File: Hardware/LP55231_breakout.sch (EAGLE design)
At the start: 13 parts

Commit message: PCB Work in progress.
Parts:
- removed LED3: LED-TRICOLOR-NO-COMPLCC-6-SMD, SparkFun-LED:LED-TRICOLOR-NO-COMPLCC-6-SMD
- added FD1, FD2: FIDUCIALUFIDUCIAL, SparkFun-Aesthetics:FIDUCIALUFIDUCIAL
- added J1, J2, J3: (no value), SparkFun-Connectors:M04NO_SILK_ALL_ROUND
- added J4: (no value), SparkFun-Connectors:M09NO_SILK
- added JP3: I2C-PULLUPS, SparkFun-Passives:JUMPER-PAD-3-NC_BY_PASTE
- added LED4: LED-TRICOLOR-5050NO_IC, SparkFun-LED:LED-TRICOLOR-5050NO_IC
- added R1, R2: 4.7K, SparkFun-Resistors:4.7KOHM-1/10W-1%(0603)
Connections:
- net N$16 renamed ADDR1
- net N$17 renamed ADDR0
- removed net N$1: LED3.RED, U$1.R3/D9
- removed net N$10: C1.1, U$1.VOUT
- removed net N$2: LED3.GRN, U$1.G3/D5
- removed net N$3: LED3.BLU, U$1.B3/D6
- removed net N$4: LED2.BLU, U$1.B2/D4
- removed net N$5: LED2.RED, U$1.R2/D8
- removed net N$6: LED2.GRN, U$1.G2/D3
- removed net N$7: LED1.RED, U$1.R1/D7
- removed net N$8: LED1.GRN, U$1.G1/D1
- removed net N$9: LED1.BLU, U$1.B1/D2
- new net B1: J1.4, LED1.BLU, U$1.B1/D2
- new net B2: J2.4, LED2.BLU, U$1.B2/D4
- new net B3: J3.4, LED4.BLU-A, U$1.B3/D6
- new net G1: J1.3, LED1.GRN, U$1.G1/D1
- new net G2: J2.3, LED2.GRN, U$1.G2/D3
- new net G3: J3.3, LED4.GRN-A, U$1.G3/D5
- new net N$15: U$1.INT
- new net N$18: U$1.TRIG
- new net N$19: U$1.EN
- new net N$20: U$1.CLK
- new net N$21: JP3.1, R2.2
- new net N$22: JP3.3, R1.2
- new net R1: J1.1, LED1.RED, U$1.R1/D7
- new net R2: J2.1, LED2.RED, U$1.R2/D8
- new net R3: J3.1, LED4.RED-A, U$1.R3/D9
- new net SCL: J4.4, R1.1, U$1.SCL
- new net SDA: J4.3, R2.1, U$1.SDA
- new net VOUT: C1.1, J4.9, U$1.VOUT
- net GND: now also J1.2, J2.2, J3.2, J4.1, LED4.BLU-C, LED4.GRN-C, LED4.RED-C; no longer LED3.BC, LED3.GC, LED3.RC
- net VCC: now also J4.2, JP3.2
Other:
- note added: "Disconnect JP3 to defeat onboard I2C pullup resistors"
- note added: "J1, J2, J3 are header pads for PTH RGB LEDs, such as COM-09264 or COM-00105"
- note added: "JP1, JP2 configure I2C Addresses: A1, A0 = address (hex) 0,0 - 0x32 0,1 - 0x33 1,0 - 0x34 1,1 - 0x35"
- note removed: "I2C Addresses: A1, A0: address (hex) 0,0 - 0x32 0,1 - 0x33 1,0 - 0x34 1,1 - 0x35"
- moved on the sheet: LED1, LED2

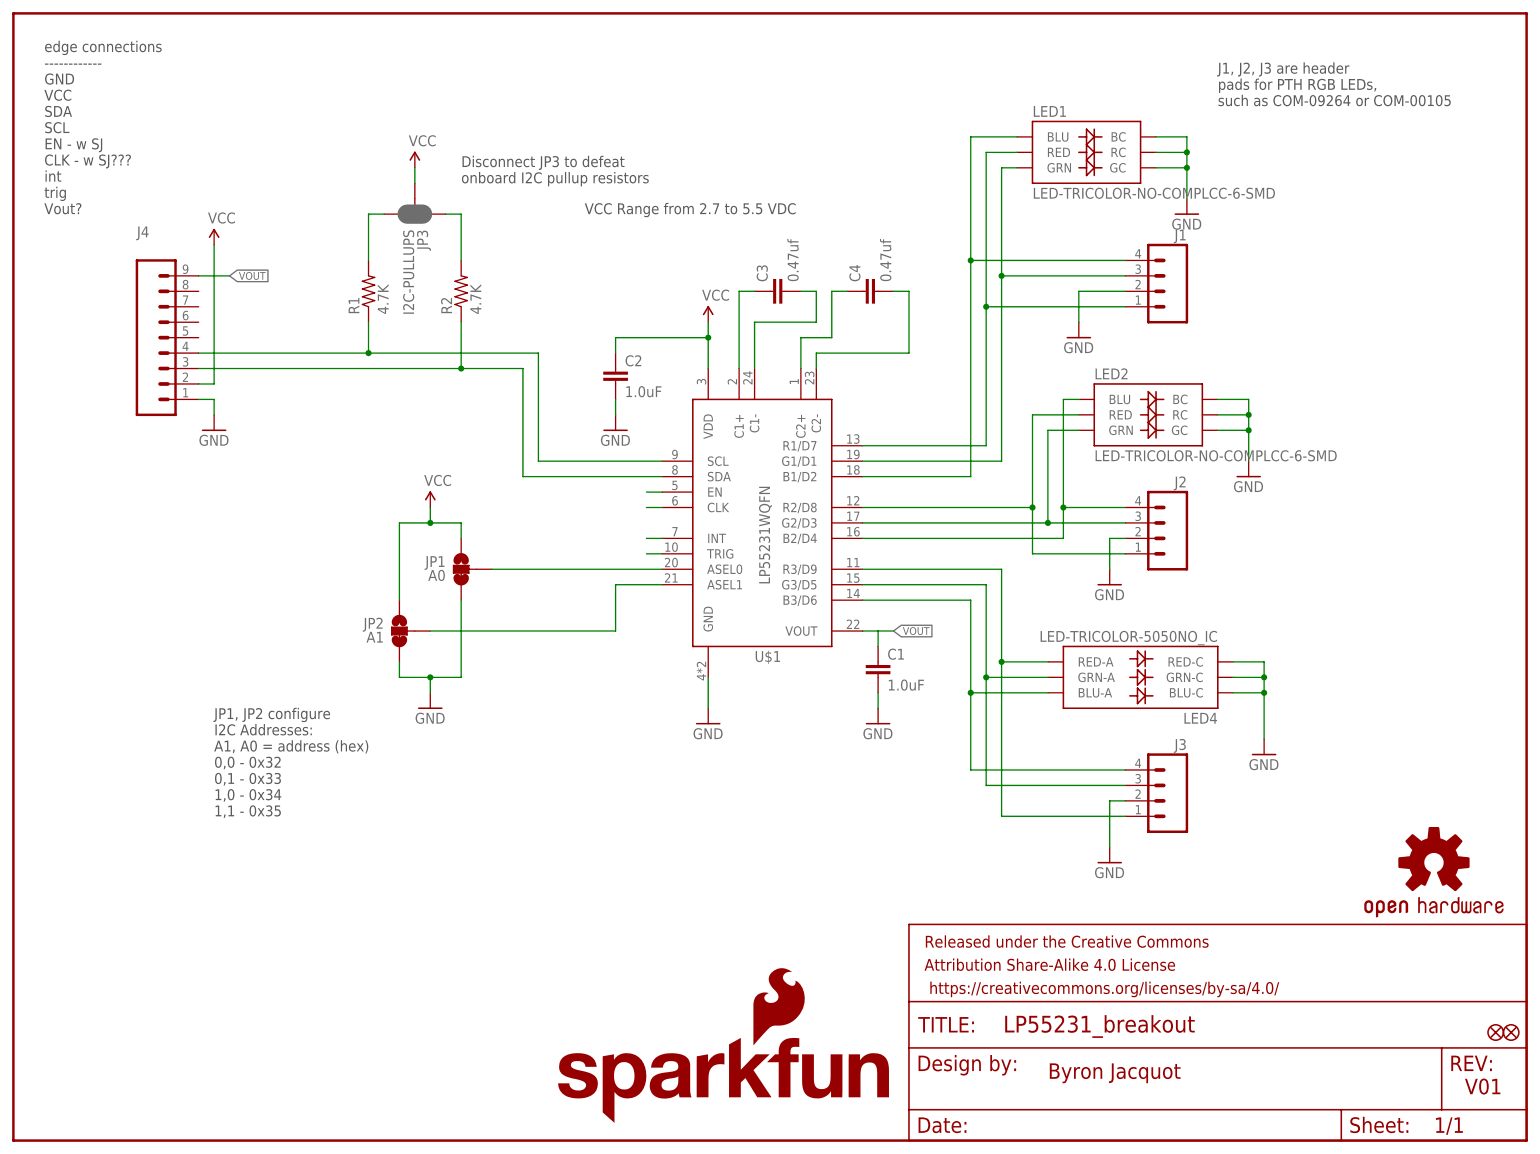
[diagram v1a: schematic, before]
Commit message: Incremental PCB routing checkin.
Eagle crashed and I'm paranoid now.
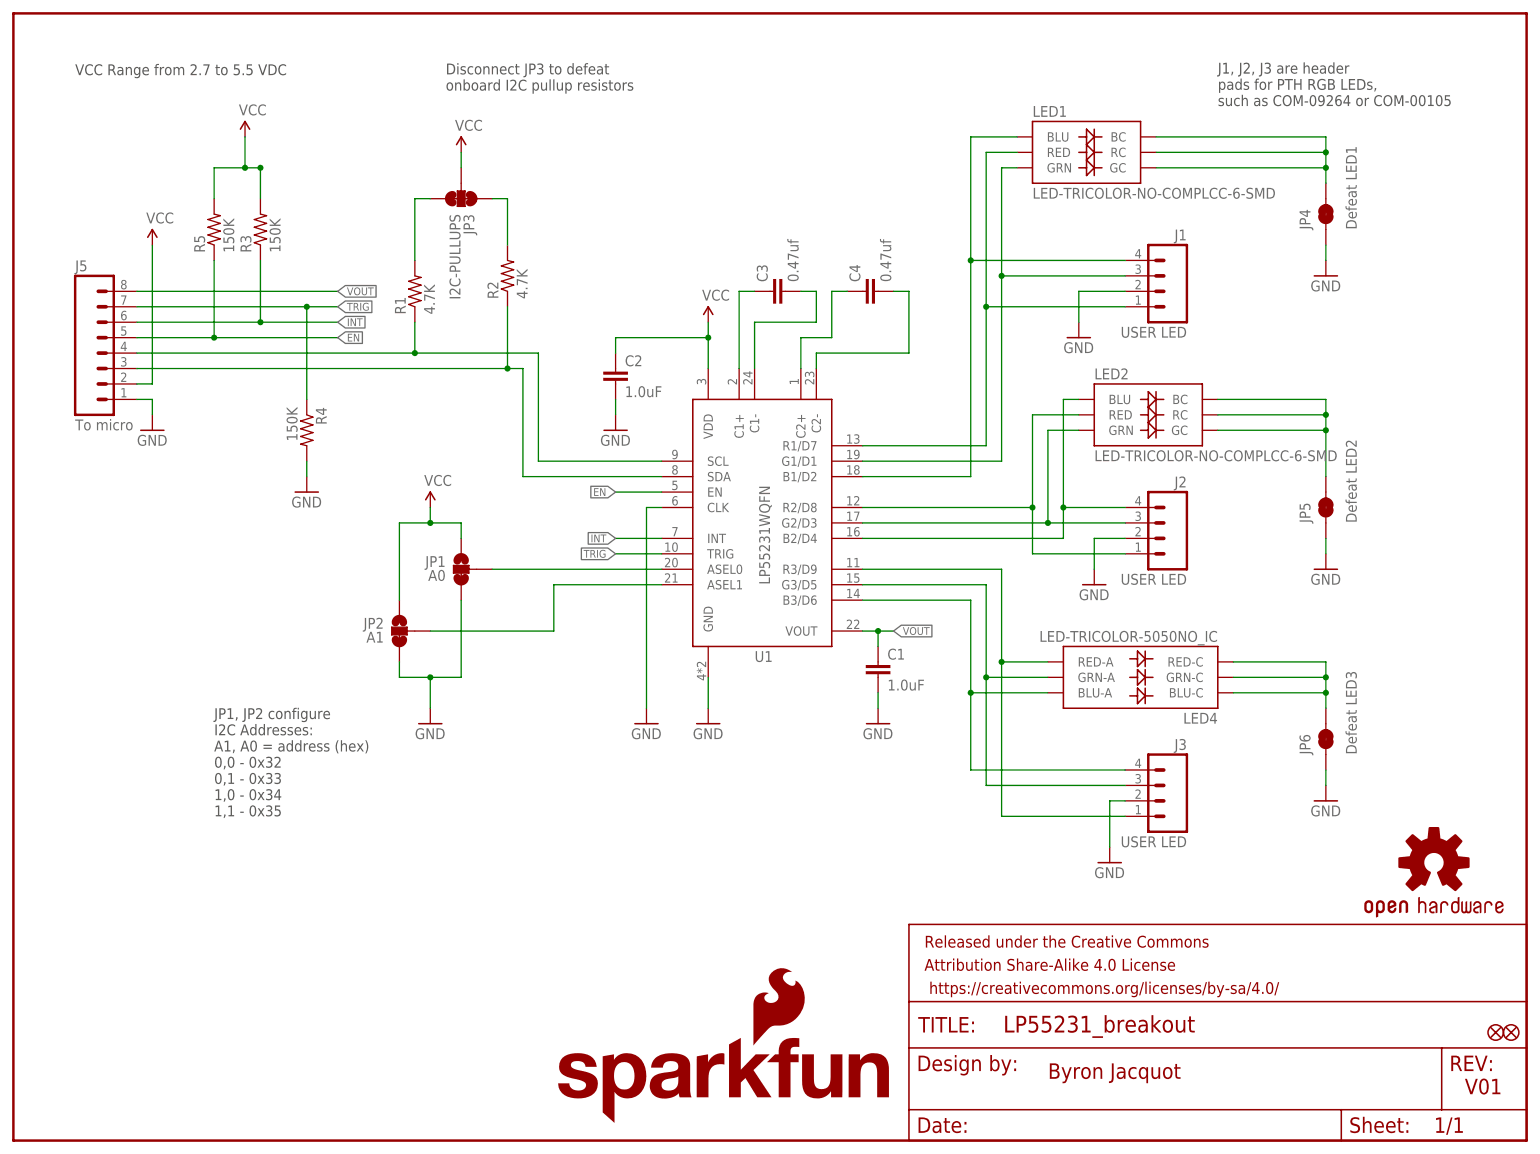
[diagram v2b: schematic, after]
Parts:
- removed J4: (no value), SparkFun-Connectors:M09NO_SILK
- added J5: To micro, SparkFun-Connectors:M08NO_SILK_FEMALE_PTH
- added JP4: Defeat LED1, SparkFun-Passives:JUMPER-PAD-2-NC_BY_TRACE
- added JP5: Defeat LED2, SparkFun-Passives:JUMPER-PAD-2-NC_BY_TRACE
- added JP6: Defeat LED3, SparkFun-Passives:JUMPER-PAD-2-NC_BY_TRACE
- added R3, R4, R5: 150K, SparkFun-Resistors:150KOHM1/10W1%(0603)
- J1, J2, J3: value (none) -> USER LED
- JP3: device SparkFun-Passives:JUMPER-PAD-3-NC_BY_PASTE -> SparkFun-Passives:JUMPER-PAD-3-NC_BY_TRACE
- renumbered U$1 to U1
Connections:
- removed net N$15: U1.INT
- removed net N$18: U1.TRIG
- removed net N$19: U1.EN
- removed net N$20: U1.CLK
- new net EN: J5.5, R5.1, U1.EN
- new net INT: J5.6, R3.1, U1.INT
- new net N$1: JP6.2, LED4.BLU-C, LED4.GRN-C, LED4.RED-C
- new net N$2: JP5.2, LED2.BC, LED2.GC, LED2.RC
- new net N$3: JP4.2, LED1.BC, LED1.GC, LED1.RC
- new net TRIG: J5.7, R4.1, U1.TRIG
- net GND: now also J5.1, JP4.1, JP5.1, JP6.1, R4.2, U1.CLK; no longer J4.1, LED1.BC, LED1.GC, LED1.RC, LED2.BC, LED2.GC, LED2.RC, LED4.BLU-C, LED4.GRN-C, LED4.RED-C
- net SCL: now also J5.4; no longer J4.4
- net SDA: now also J5.3; no longer J4.3
- net VCC: now also J5.2, R3.2, R5.2; no longer J4.2
- net VOUT: now also J5.8; no longer J4.9
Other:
- note removed: "edge connections ------------ GND VCC SDA SCL EN - w SJ CLK - w SJ??? int trig Vout?"
- moved on the sheet: R1, R2

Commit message: Routing approaching completion.
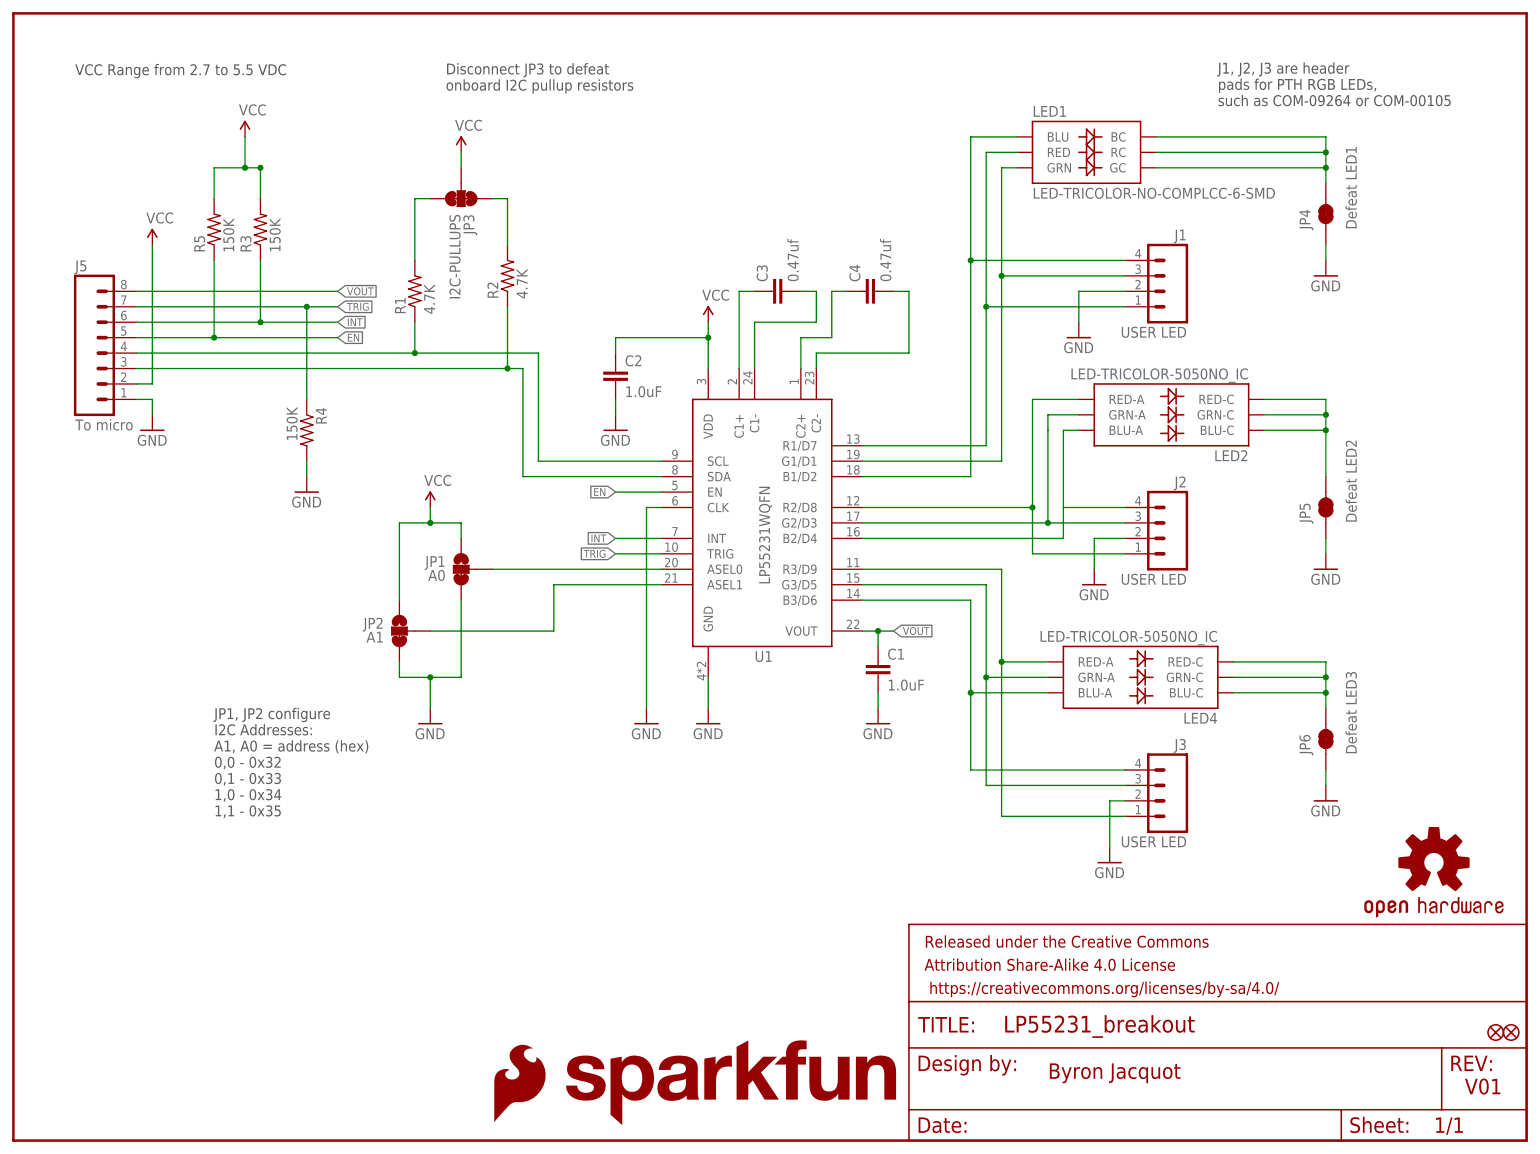
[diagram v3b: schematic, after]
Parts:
- added LOGO3: SFE_LOGO_FLAME.1_INCH, SparkFun-Aesthetics:SFE_LOGO_FLAME.1_INCH
- JP4, JP5, JP6: device SparkFun-Passives:JUMPER-PAD-2-NC_BY_TRACE -> SparkFun-Passives:JUMPER-PAD-2-NC_BY_TRACENO_SILK
- LED2: value LED-TRICOLOR-NO-COMPLCC-6-SMD -> LED-TRICOLOR-5050NO_IC; device SparkFun-LED:LED-TRICOLOR-NO-COMPLCC-6-SMD -> SparkFun-LED:LED-TRICOLOR-5050NO_IC
- LOGO2: value SFE_LOGO_NAME_FLAME.1_INCH -> SFE_LOGO_NAME.1_INCH; device SparkFun-Aesthetics:SFE_LOGO_NAME_FLAME.1_INCH -> SparkFun-Aesthetics:SFE_LOGO_NAME.1_INCH
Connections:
- net B2: now also LED2.BLU-A; no longer LED2.BLU
- net G2: now also LED2.GRN-A; no longer LED2.GRN
- net N$2: now also LED2.BLU-C, LED2.GRN-C, LED2.RED-C; no longer LED2.BC, LED2.GC, LED2.RC
- net R2: now also LED2.RED-A; no longer LED2.RED
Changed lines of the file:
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@@
 <part name="SUPPLY1" library="SparkFun-Aesthetics" deviceset="VCC" device=""/>
 <part name="LED1" library="SparkFun-LED" deviceset="LED-TRICOLOR-NO-COM" device="PLCC-6-SMD"/>
-<part name="LED2" library="SparkFun-LED" deviceset="LED-TRICOLOR-NO-COM" device="PLCC-6-SMD"/>
 <part name="C1" library="SparkFun-Capacitors" deviceset="1.0UF-16V-10%(0603)" device="" value="1.0uF"/>
 <part name="C2" library="SparkFun-Capacitors" deviceset="1.0UF-16V-10%(0603)" device="" value="1.0uF"/>
@@
 <part name="SUPPLY2" library="SparkFun-Aesthetics" deviceset="VCC" device=""/>
 <part name="LOGO1" library="SparkFun-Aesthetics" deviceset="OSHW-LOGO" device="S"/>
-<part name="LOGO2" library="SparkFun-Aesthetics" deviceset="SFE_LOGO_NAME_FLAME" device=".1_INCH"/>
+<part name="LOGO2" library="SparkFun-Aesthetics" deviceset="SFE_LOGO_NAME" device=".1_INCH"/>
 <part name="LED4" library="SparkFun-LED" deviceset="LED-TRICOLOR-5050" device="NO_IC"/>
 <part name="J1" library="SparkFun-Connectors" deviceset="M04" device="NO_SILK_ALL_ROUND" value="USER LED"/>
@@
 <part name="FD2" library="SparkFun-Aesthetics" deviceset="FIDUCIAL" device="UFIDUCIAL"/>
 <part name="GND12" library="SparkFun-Aesthetics" deviceset="GND" device=""/>
-<part name="JP4" library="SparkFun-Passives" deviceset="JUMPER-PAD-2-NC_BY_TRACE" device="" value="Defeat LED1"/>
-<part name="JP5" library="SparkFun-Passives" deviceset="JUMPER-PAD-2-NC_BY_TRACE" device="" value="Defeat LED2"/>
-<part name="JP6" library="SparkFun-Passives" deviceset="JUMPER-PAD-2-NC_BY_TRACE" device="" value="Defeat LED3"/>
+<part name="JP4" library="SparkFun-Passives" deviceset="JUMPER-PAD-2-NC_BY_TRACE" device="NO_SILK" value="Defeat LED1"/>
+<part name="JP5" library="SparkFun-Passives" deviceset="JUMPER-PAD-2-NC_BY_TRACE" device="NO_SILK" value="Defeat LED2"/>
+<part name="JP6" library="SparkFun-Passives" deviceset="JUMPER-PAD-2-NC_BY_TRACE" device="NO_SILK" value="Defeat LED3"/>
 <part name="J5" library="SparkFun-Connectors" deviceset="M08" device="NO_SILK_FEMALE_PTH" value="To micro"/>
 <part name="R3" library="SparkFun-Resistors" deviceset="150KOHM1/10W1%(0603)" device="" value="150K"/>
@@
 <part name="R5" library="SparkFun-Resistors" deviceset="150KOHM1/10W1%(0603)" device="" value="150K"/>
 <part name="GND13" library="SparkFun-Aesthetics" deviceset="GND" device=""/>
+<part name="LOGO3" library="SparkFun-Aesthetics" deviceset="SFE_LOGO_FLAME" device=".1_INCH"/>
+<part name="LED2" library="SparkFun-LED" deviceset="LED-TRICOLOR-5050" device="NO_IC"/>
 </parts>
 <sheets>
@@
 <instance part="SUPPLY1" gate="G$1" x="114.3" y="134.62"/>
 <instance part="LED1" gate="G$1" x="177.8" y="162.56"/>
-<instance part="LED2" gate="G$1" x="187.96" y="119.38"/>
 <instance part="C1" gate="G$1" x="142.24" y="76.2"/>
 <instance part="C2" gate="G$1" x="99.06" y="124.46"/>
@@
 <instance part="R5" gate="G$1" x="33.02" y="149.86" rot="R90"/>
 <instance part="GND13" gate="1" x="48.26" y="106.68"/>
+<instance part="LOGO3" gate="G$1" x="78.74" y="2.54"/>
+<instance part="LED2" gate="D1" x="190.5" y="119.38" rot="R180"/>
 </instances>
 <busses>
@@
 <wire x1="139.7" y1="99.06" x2="172.72" y2="99.06" width="0.1524" layer="91"/>
 <wire x1="172.72" y1="99.06" x2="172.72" y2="104.14" width="0.1524" layer="91"/>
-<pinref part="LED2" gate="G$1" pin="BLU"/>
-<wire x1="172.72" y1="104.14" x2="172.72" y2="121.92" width="0.1524" layer="91"/>
-<wire x1="172.72" y1="121.92" x2="175.26" y2="121.92" width="0.1524" layer="91"/>
 <pinref part="J2" gate="G$1" pin="4"/>
 <wire x1="182.88" y1="104.14" x2="172.72" y2="104.14" width="0.1524" layer="91"/>
-<junction x="172.72" y="104.14"/>
+<wire x1="172.72" y1="104.14" x2="172.72" y2="116.84" width="0.2032" layer="91"/>
+<pinref part="LED2" gate="D1" pin="BLU-A"/>
+<wire x1="172.72" y1="116.84" x2="175.26" y2="116.84" width="0.2032" layer="91"/>
 </segment>
 </net>
 <net name="R2" class="0">
 <segment>
-<pinref part="LED2" gate="G$1" pin="RED"/>
 <pinref part="U1" gate="G$1" pin="R2/D8"/>
-<wire x1="175.26" y1="119.38" x2="167.64" y2="119.38" width="0.1524" layer="91"/>
 <wire x1="167.64" y1="119.38" x2="167.64" y2="104.14" width="0.1524" layer="91"/>
 <wire x1="167.64" y1="104.14" x2="139.7" y2="104.14" width="0.1524" layer="91"/>
@@
 <wire x1="167.64" y1="96.52" x2="167.64" y2="104.14" width="0.1524" layer="91"/>
 <junction x="167.64" y="104.14"/>
+<wire x1="167.64" y1="119.38" x2="167.64" y2="121.92" width="0.2032" layer="91"/>
+<pinref part="LED2" gate="D1" pin="RED-A"/>
+<wire x1="167.64" y1="121.92" x2="175.26" y2="121.92" width="0.2032" layer="91"/>
 </segment>
 </net>
@@
 <segment>
 <pinref part="U1" gate="G$1" pin="G2/D3"/>
-<pinref part="LED2" gate="G$1" pin="GRN"/>
 <wire x1="139.7" y1="101.6" x2="170.18" y2="101.6" width="0.1524" layer="91"/>
 <wire x1="170.18" y1="101.6" x2="170.18" y2="116.84" width="0.1524" layer="91"/>
-<wire x1="170.18" y1="116.84" x2="175.26" y2="116.84" width="0.1524" layer="91"/>
 <pinref part="J2" gate="G$1" pin="3"/>
 <wire x1="170.18" y1="101.6" x2="182.88" y2="101.6" width="0.1524" layer="91"/>
 <junction x="170.18" y="101.6"/>
+<wire x1="170.18" y1="116.84" x2="170.18" y2="119.38" width="0.2032" layer="91"/>
+<pinref part="LED2" gate="D1" pin="GRN-A"/>
+<wire x1="170.18" y1="119.38" x2="175.26" y2="119.38" width="0.2032" layer="91"/>
 </segment>
 </net>
@@
 <net name="N$2" class="0">
 <segment>
-<pinref part="LED2" gate="G$1" pin="BC"/>
-<wire x1="198.12" y1="121.92" x2="215.9" y2="121.92" width="0.1524" layer="91"/>
+<wire x1="205.74" y1="121.92" x2="215.9" y2="121.92" width="0.1524" layer="91"/>
 <wire x1="215.9" y1="121.92" x2="215.9" y2="119.38" width="0.1524" layer="91"/>
-<pinref part="LED2" gate="G$1" pin="RC"/>
 <wire x1="215.9" y1="119.38" x2="215.9" y2="116.84" width="0.1524" layer="91"/>
-<wire x1="198.12" y1="119.38" x2="215.9" y2="119.38" width="0.1524" layer="91"/>
 <junction x="215.9" y="119.38"/>
-<pinref part="LED2" gate="G$1" pin="GC"/>
-<wire x1="198.12" y1="116.84" x2="215.9" y2="116.84" width="0.1524" layer="91"/>
+<wire x1="205.74" y1="119.38" x2="215.9" y2="119.38" width="0.1524" layer="91"/>
 <pinref part="JP5" gate="G$1" pin="2"/>
+<wire x1="205.74" y1="116.84" x2="215.9" y2="116.84" width="0.1524" layer="91"/>
 <wire x1="215.9" y1="116.84" x2="215.9" y2="109.22" width="0.1524" layer="91"/>
 <junction x="215.9" y="116.84"/>
-</segment>
-</net>
+<pinref part="LED2" gate="D1" pin="BLU-C"/>
+<pinref part="LED2" gate="D1" pin="GRN-C"/>
+<pinref part="LED2" gate="D1" pin="RED-C"/>
+</segment>
+</net>
